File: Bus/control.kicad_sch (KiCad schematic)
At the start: 2 parts, among them J6 Conn_01x10_Pin, J7 Conn_01x04_Pin

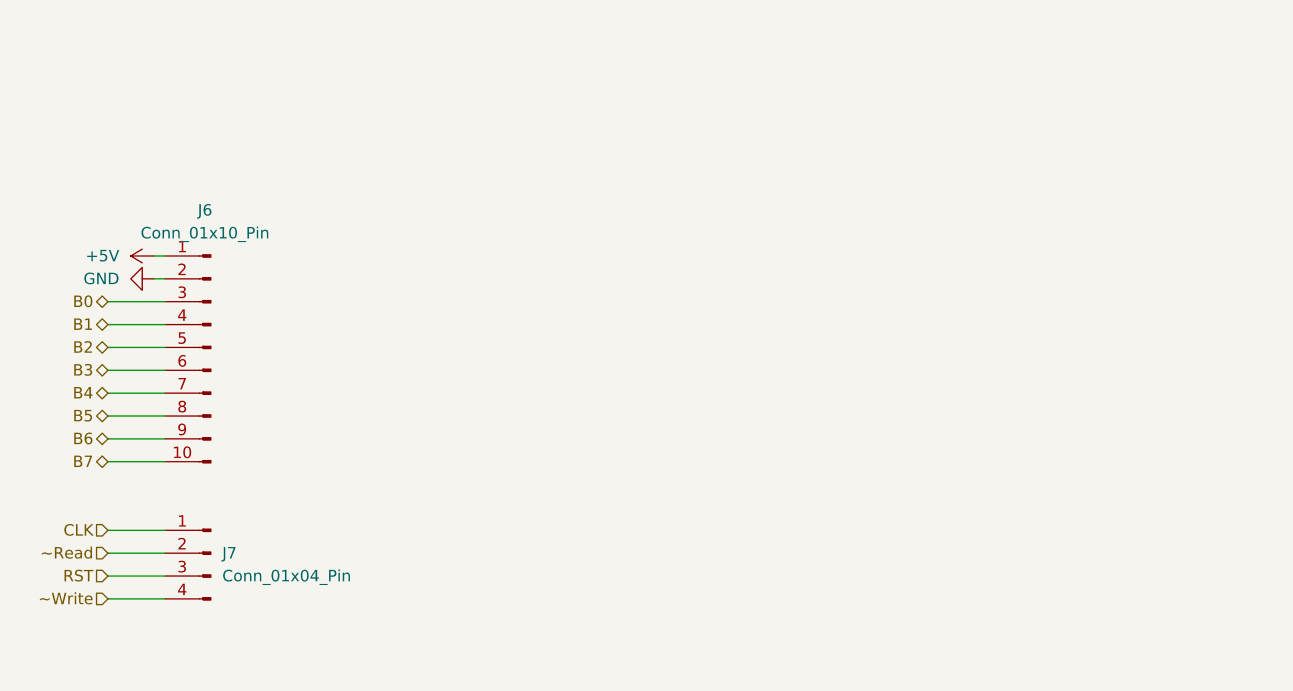
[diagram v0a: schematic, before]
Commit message: Updated bus schematics with pinout of MAR/ALU/Registers on PCBs ordered
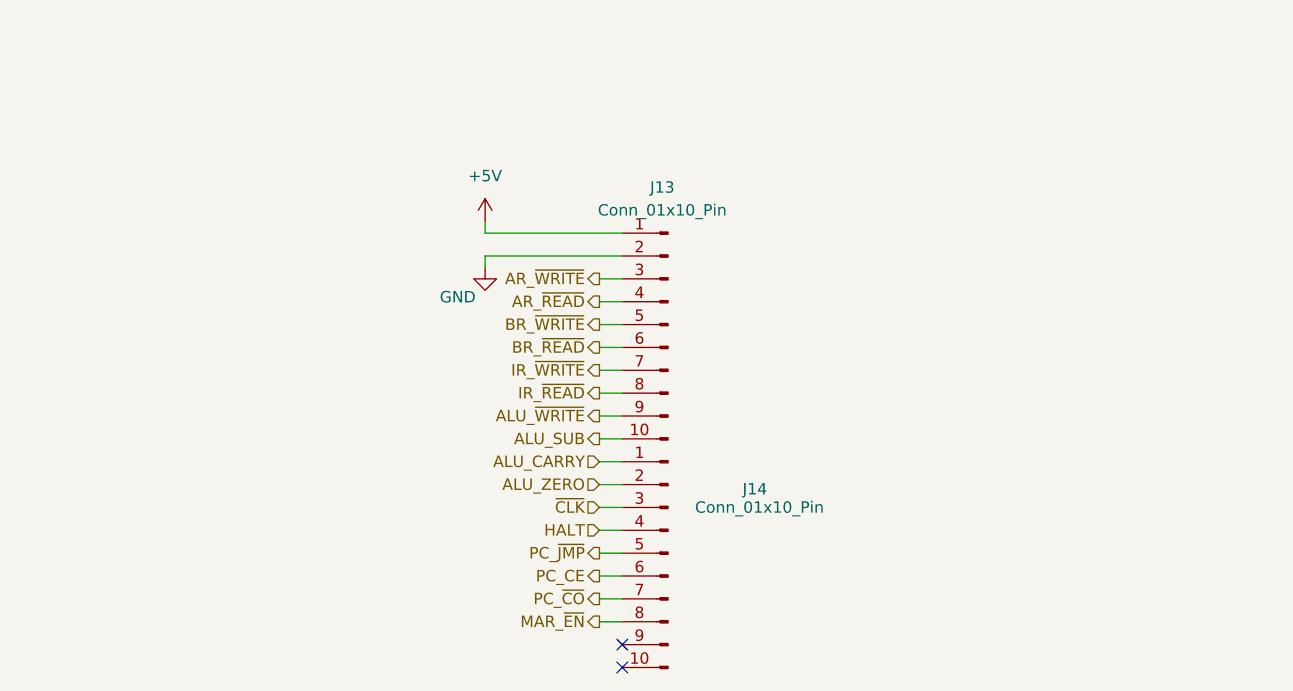
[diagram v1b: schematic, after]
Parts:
- removed J6: Conn_01x10_Pin, Connector_PinHeader_2.54mm:PinHeader_1x10_P2.54mm_Vertical, symbol Connector:Conn_01x10_Pin
- removed J7: Conn_01x04_Pin, Connector_PinHeader_2.54mm:PinHeader_1x04_P2.54mm_Vertical, symbol Connector:Conn_01x04_Pin
- added J13, J14: Conn_01x10_Pin, Connector_PinHeader_2.54mm:PinHeader_1x10_P2.54mm_Vertical, symbol Connector:Conn_01x10_Pin
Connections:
- net +5V: now also J13.1 (Pin_1)
- net GND: now also J13.2 (Pin_2)
- new net ALU_CARRY: J14.1 (Pin_1)
- new net ALU_SUB: J13.10 (Pin_10)
- new net ALU_ZERO: J14.2 (Pin_2)
- new net ALU_~{WRITE}: J13.9 (Pin_9)
- new net AR_~{READ}: J13.4 (Pin_4)
- new net AR_~{WRITE}: J13.3 (Pin_3)
- new net BR_~{READ}: J13.6 (Pin_6)
- new net BR_~{WRITE}: J13.5 (Pin_5)
- new net HALT: J14.4 (Pin_4)
- new net IR_~{READ}: J13.8 (Pin_8)
- new net IR_~{WRITE}: J13.7 (Pin_7)
- new net MAR_~{EN}: J14.8 (Pin_8)
- new net PC_CE: J14.6 (Pin_6)
- new net PC_~{CO}: J14.7 (Pin_7)
- new net PC_~{JMP}: J14.5 (Pin_5)
- new net ~{CLK}: J14.3 (Pin_3)
- no-connect marks 0 -> 2

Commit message: Updated bus schematic control pins and added spare bus connection
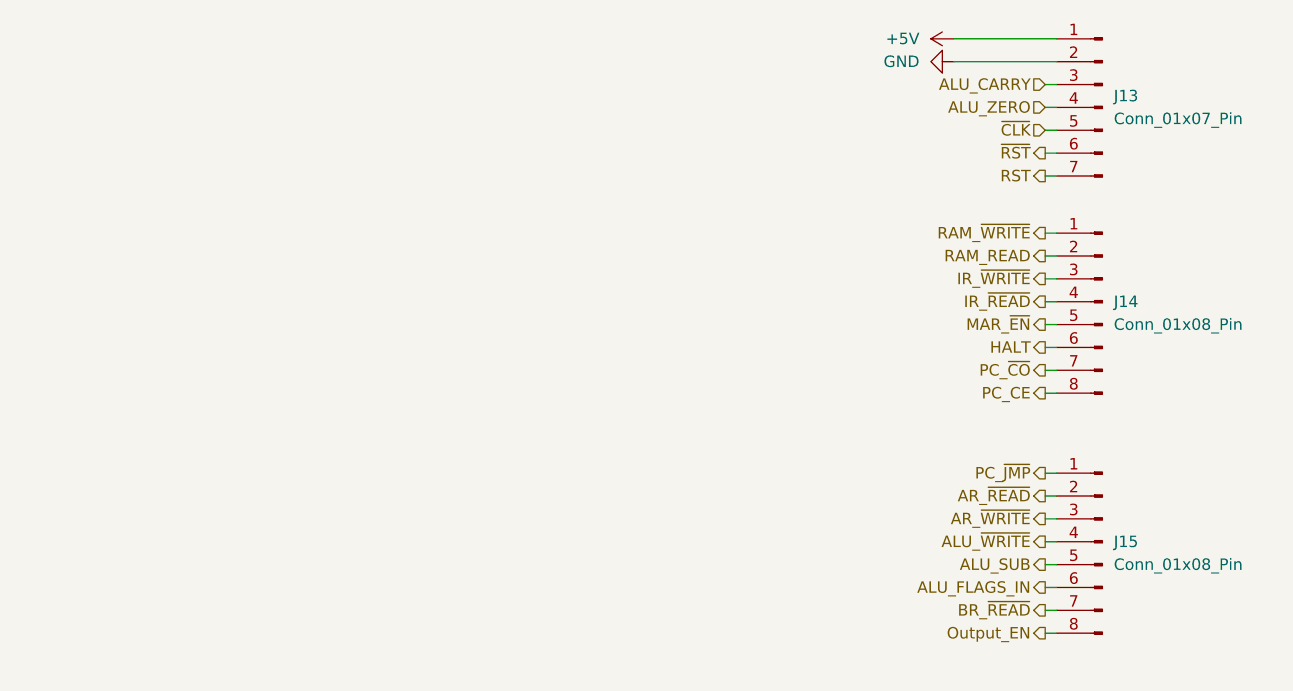
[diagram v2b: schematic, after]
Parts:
- removed J13, J14: Conn_01x10_Pin, Connector_PinHeader_2.54mm:PinHeader_1x10_P2.54mm_Vertical, symbol Connector:Conn_01x10_Pin
- added J13: Conn_01x07_Pin, Connector_PinHeader_2.54mm:PinHeader_1x07_P2.54mm_Vertical, symbol Connector:Conn_01x07_Pin
- added J14, J15: Conn_01x08_Pin, Connector_PinHeader_2.54mm:PinHeader_1x08_P2.54mm_Vertical, symbol Connector:Conn_01x08_Pin
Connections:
- net +5V: now also J13.1 (Pin_1)
- net ALU_CARRY: now also J13.3 (Pin_3)
- net ALU_SUB: now also J15.5 (Pin_5)
- net ALU_ZERO: now also J13.4 (Pin_4)
- net ALU_~{WRITE}: now also J15.4 (Pin_4)
- net AR_~{READ}: now also J15.2 (Pin_2)
- net AR_~{WRITE}: now also J15.3 (Pin_3)
- net BR_~{READ}: now also J15.7 (Pin_7)
- net GND: now also J13.2 (Pin_2)
- net HALT: now also J14.6 (Pin_6)
- net IR_~{READ}: now also J14.4 (Pin_4)
- net IR_~{WRITE}: now also J14.3 (Pin_3)
- net MAR_~{EN}: now also J14.5 (Pin_5)
- net PC_CE: now also J14.8 (Pin_8)
- net PC_~{CO}: now also J14.7 (Pin_7)
- net PC_~{JMP}: now also J15.1 (Pin_1)
- net ~{CLK}: now also J13.5 (Pin_5)
- new net ALU_FLAGS_IN: J15.6 (Pin_6)
- new net Output_EN: J15.8 (Pin_8)
- new net RAM_READ: J14.2 (Pin_2)
- new net RAM_~{WRITE}: J14.1 (Pin_1)
- new net RST: J13.7 (Pin_7)
- new net ~{RST}: J13.6 (Pin_6)
- no-connect marks 2 -> 0
